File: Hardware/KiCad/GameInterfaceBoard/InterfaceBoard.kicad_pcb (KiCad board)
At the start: 2 copper layers, 22 parts, among them J1 CONN_11LOCK, J2 CONN_07LOCK

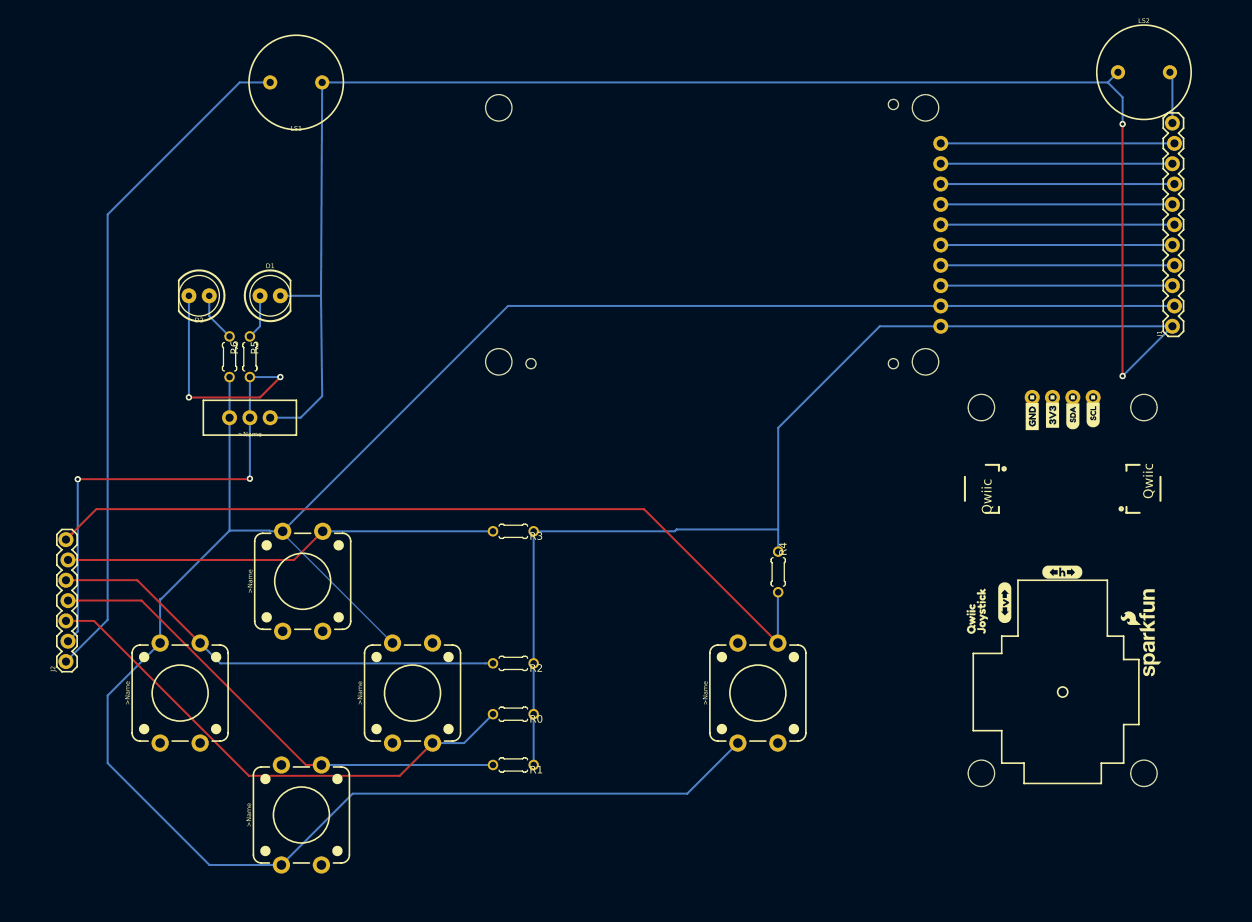
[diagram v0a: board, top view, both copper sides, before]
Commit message: Added Silk Screen, board outline and updated KiCad frame as indicated on issue #2
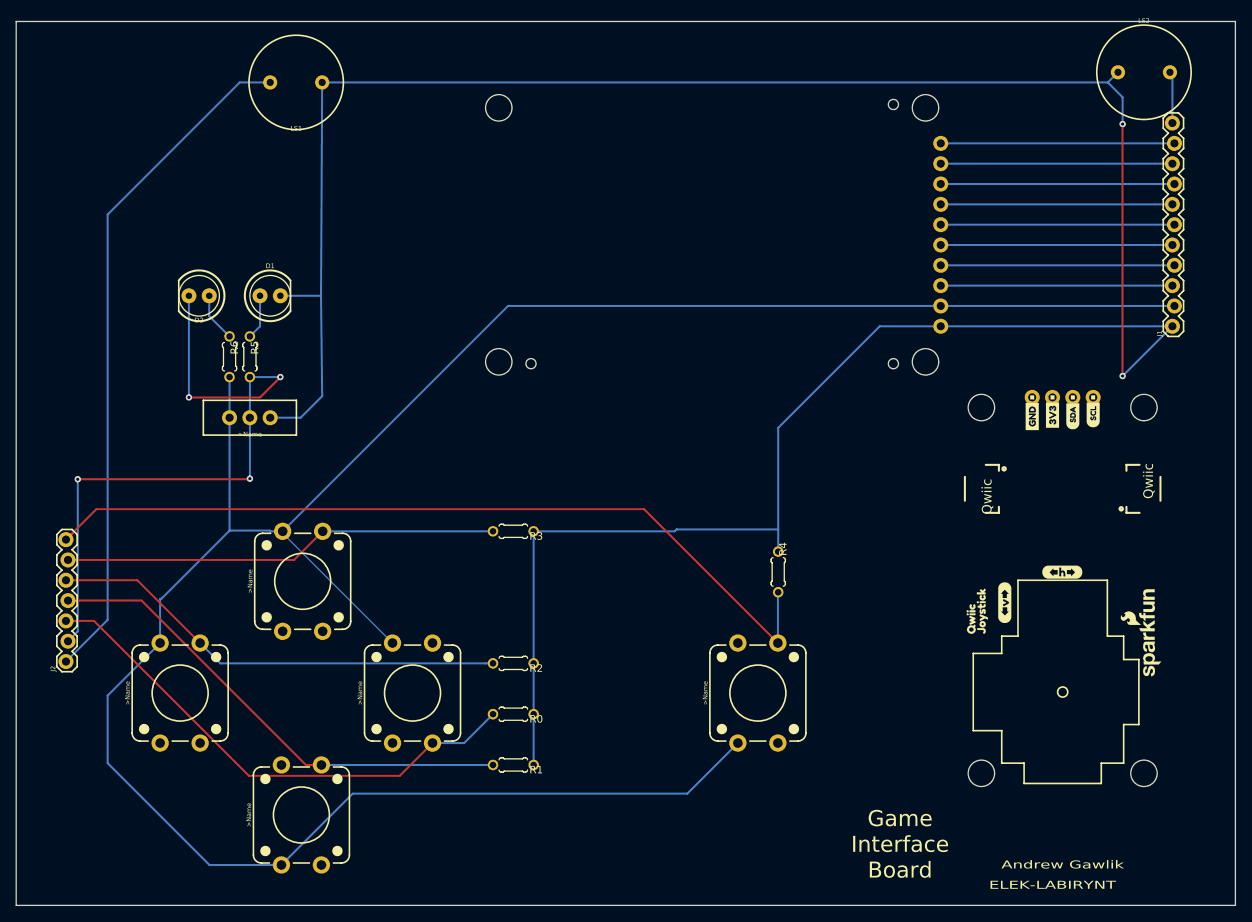
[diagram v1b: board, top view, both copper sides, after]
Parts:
- moved FRAME1 268.6 mm to (202.5, 175.5)
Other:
- board outline added: 152.4 x 110.5 mm
- board text added: "ELEK-LABIRYNT"
- board text added: "Game Interface Board"

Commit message: Added drill holes for issue #2
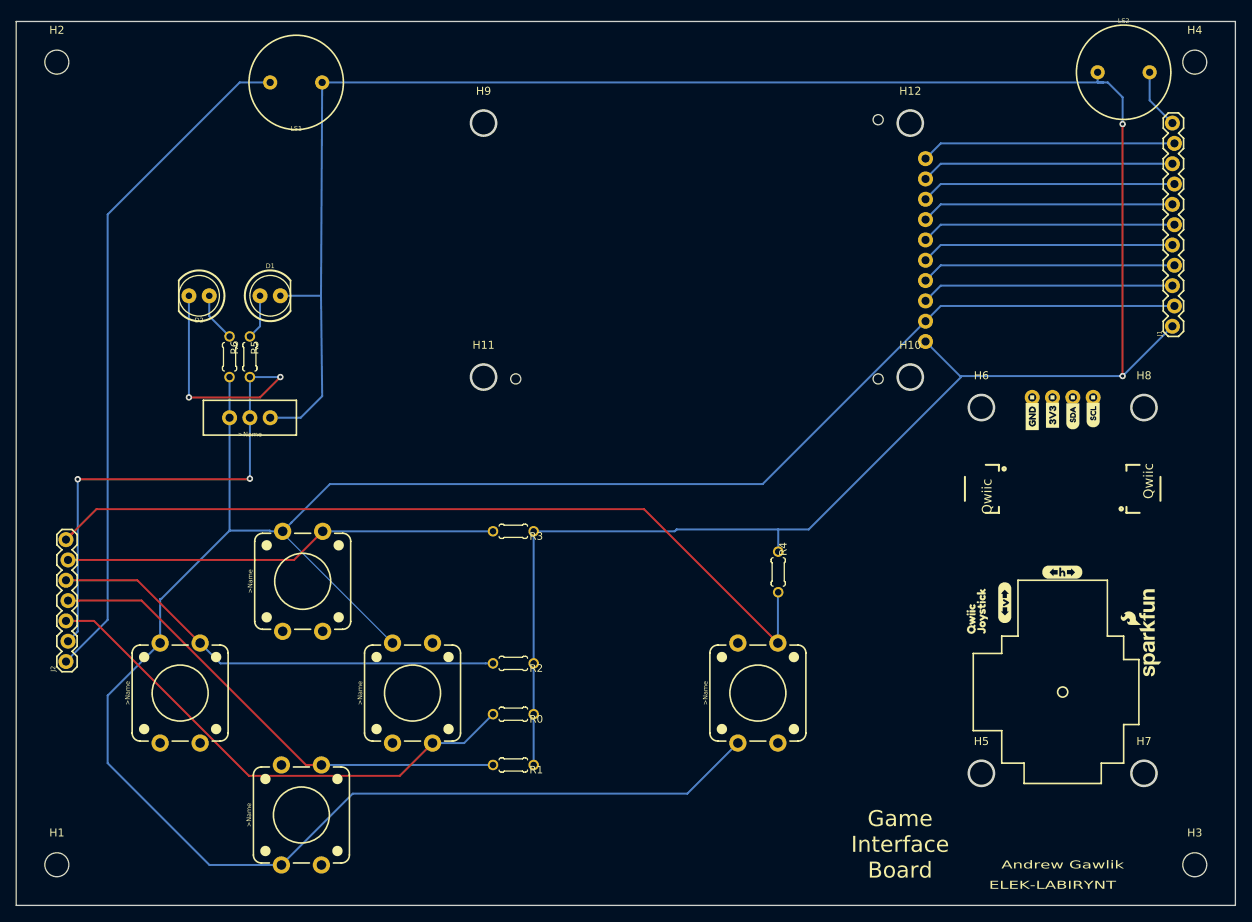
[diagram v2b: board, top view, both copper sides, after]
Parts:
- added FRAME1: FRAME-LETTER, InterfaceBoard:CREATIVE_COMMONS, F.Cu at (54.9, 38.4)
- added FRAME2: FRAME-LETTER, InterfaceBoard:CREATIVE_COMMONS, F.Cu at (56.4, 38.4)
- added FRAME3: FRAME-LETTER, InterfaceBoard:CREATIVE_COMMONS, F.Cu at (57.9, 38.4)
- added H1: MountingHole, MountingHole:MountingHole_3mm, F.Cu at (77.5, 141.0)
- added H10: MountingHole, MountingHole:MountingHole_3mm, F.Cu at (184.2, 80.0)
- added H11: MountingHole, MountingHole:MountingHole_3mm, F.Cu at (130.8, 80.0)
- added H12: MountingHole, MountingHole:MountingHole_3mm, F.Cu at (184.2, 48.3)
- added H2: MountingHole, MountingHole:MountingHole_3mm, F.Cu at (77.5, 40.6)
- added H3: MountingHole, MountingHole:MountingHole_3mm, F.Cu at (219.7, 141.0)
- added H4: MountingHole, MountingHole:MountingHole_3mm, F.Cu at (219.7, 40.6)
- added H5: MountingHole, MountingHole:MountingHole_3mm, F.Cu at (193.0, 129.5)
- added H6: MountingHole, MountingHole:MountingHole_3mm, F.Cu at (193.0, 83.8)
- added H7: MountingHole, MountingHole:MountingHole_3mm, F.Cu at (213.4, 129.5)
- added H8: MountingHole, MountingHole:MountingHole_3mm, F.Cu at (213.4, 83.8)
- added H9: MountingHole, MountingHole:MountingHole_3mm, F.Cu at (130.8, 48.3)
- moved A2 2.69 mm to (187.3, 83.2)
- moved LS2 2.54 mm to (210.8, 41.9)
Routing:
- net GND: track 328.4 -> 318.7 mm
- net /TE: track 29.0 -> 31.7 mm
- net /SDCS: track 29.2 -> 31.9 mm
- net /PWM: track 29.0 -> 31.7 mm
- net /COPI: track 29.0 -> 31.7 mm
- net /CIPO: track 29.2 -> 31.9 mm
- net /LCDCS: track 29.0 -> 31.7 mm
- net /DC: track 29.2 -> 31.9 mm
- net /SCLK: track 29.2 -> 31.9 mm
- net /RSPK: track 6.48 -> 7.53 mm
